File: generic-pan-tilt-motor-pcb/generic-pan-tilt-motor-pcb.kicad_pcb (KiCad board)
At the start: 2 copper layers, 73 x 28 mm, 76 parts, among them J1 B12B-PH-SM4-TBT, J2 S4B-PH-SM4-TB, J3 S4B-PH-SM4-TB, J4 1945096, J5 1945119, J6 1945151, Q1 DMN6075S, U1 TMC5240ATJ+, U2 MCP23S08-xSO, U3 74LVC3G17

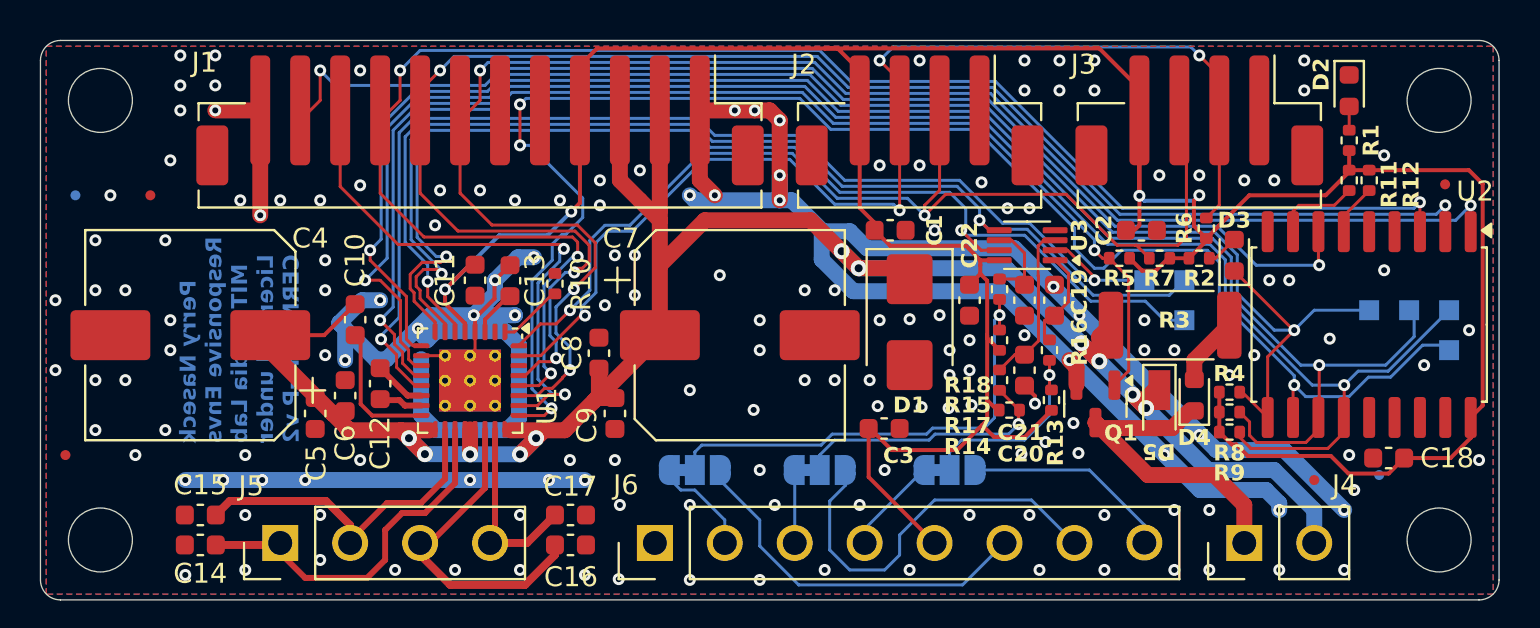
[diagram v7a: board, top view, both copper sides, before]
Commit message: motor fix flipped spi mcp, spi tristate for drc, silk screw terminals, all parts manf and vendors
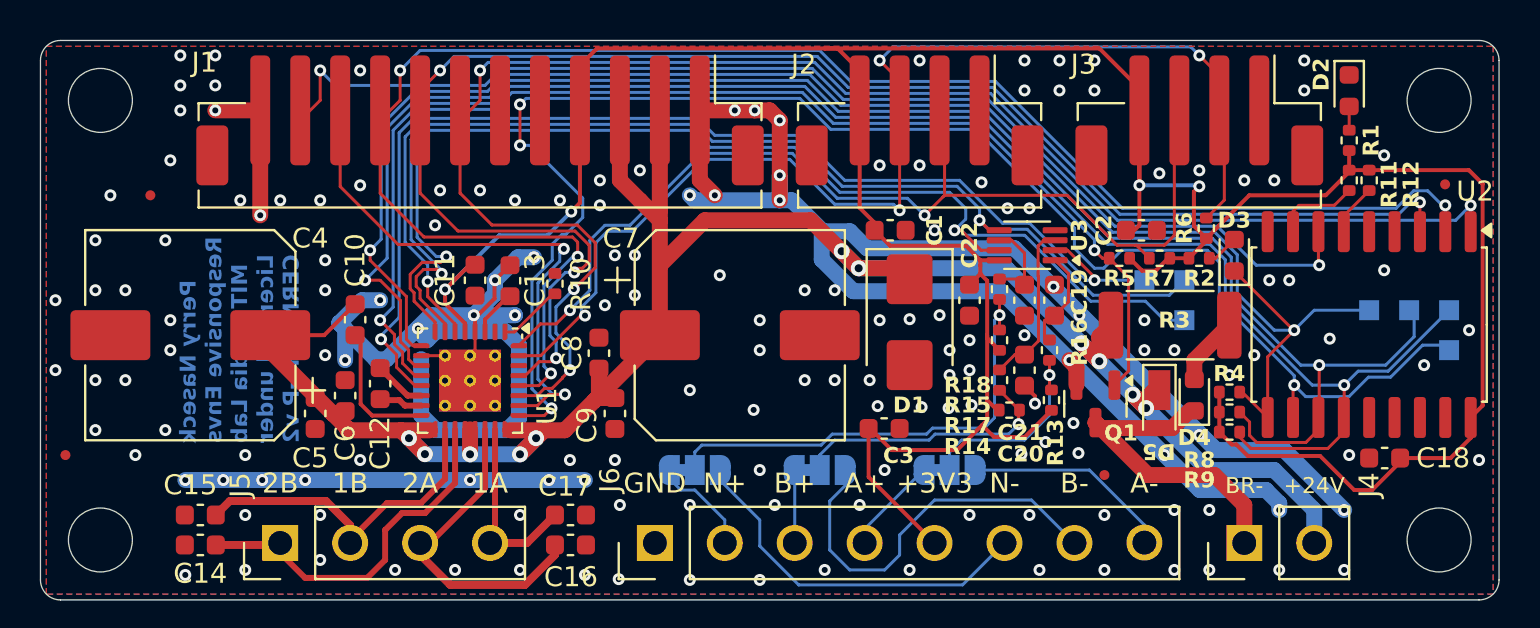
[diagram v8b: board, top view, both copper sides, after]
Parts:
- removed FID5, FID6: Fiducial, Fiducial:Fiducial_0.5mm_Mask1mm
- C1, C2, C3: value 1µF 16V -> 1µF
- C10, C6, C9: value 1uF 50V -> 1µF
- C11: value 0.1uF 16V -> 0.1µF
- C12: value 22nF 50V -> 22nF
- C13: value 2.2uF 16V -> 2.2uF
- C14, C15, C16, C17: value 1nF 100V -> 1nF
- C18, C22: value 0.1µF 16V -> 0.1µF
- C19, C20, C21: value 15pF 50V -> 15pF
- C4, C7: value 150uF 50V -> 150uF
- C5, C8: value 0.1uF 50V -> 0.1µF
- J1: value B12B-PH-SM4-TBT -> B12B-PH-SM4-TB
- J2, J3: value S4B-PH-SM4-TB -> B4B-PH-SM4-TB
- R1, R2: value 55Ω -> 56Ω
- R3: value 1.2kΩ 1W -> 1.2kΩ
- moved FID4 10.5 mm to (148.2, 111.8)
- moved C18 0.20 mm to (162.3, 110.9)
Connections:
- U2 pad 2: /SPI_POCI -> /SPI_PICO
- U2 pad 3: /SPI_PICO -> /SPI_POCI
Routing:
- net /REF_R: track 54.3 -> 52.4 mm
- net /SPI_PICO: track 83.2 -> 84.9 mm
- net /SPI_POCI: track 80.9 -> 79.8 mm
- net /ENC_A_FILTERED: track 58.1 -> 58.9 mm
- net +3V3: track 162.1 -> 162.6 mm
- net GND: vias 167 -> 166
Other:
- board text added: "+24V"
- board text added: "+3V3"
- board text added: "1A"
- board text added: "1B"
- board text added: "2A"
- board text added: "2B"
- board text added: "A+"
- board text added: "A-"
- board text added: "B+"
- board text added: "B-"
- board text added: "BR-"
- board text added: "GND"
- board text added: "N+"
- board text added: "N-"
